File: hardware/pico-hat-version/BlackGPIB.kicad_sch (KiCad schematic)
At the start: 7 parts, among them J1 SD_Card_Module, J2 Raspberry_Pi_Connector

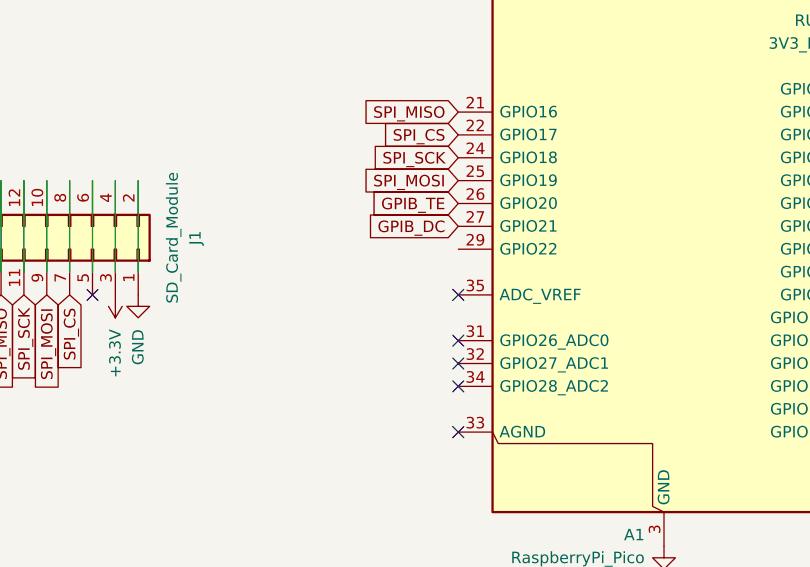
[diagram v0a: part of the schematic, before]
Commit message: fix pico hatted version: swap dc te and fix dc te on schematic
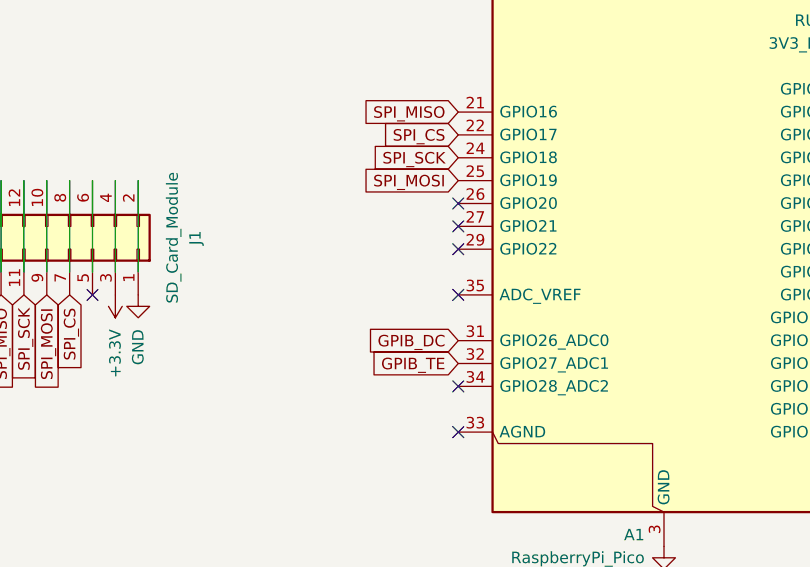
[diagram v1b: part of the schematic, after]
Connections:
- net GPIB_DC: now also A1.31 (GPIO26_ADC0); no longer A1.27 (GPIO21)
- net GPIB_TE: now also A1.32 (GPIO27_ADC1); no longer A1.26 (GPIO20)
- no-connect marks 8 -> 9

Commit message: pcb
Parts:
- A1: footprint Module:RaspberryPi_Pico_Common_Unspecified -> Module:RaspberryPi_Pico_W_SMD_HandSolder
- J1: footprint (none) -> Connector_PinHeader_2.54mm:PinHeader_2x08_P2.54mm_Vertical_SMD
- J2: footprint (none) -> Connector_PinHeader_2.54mm:PinHeader_2x20_P2.54mm_Vertical_SMD
- RN1, RN4: footprint Resistor_THT:R_Array_SIP9 -> custom:PinHeader_1x09_P2.54mm_Horizontal_Left
- RN2, RN3: footprint Resistor_THT:R_Array_SIP9 -> custom:PinHeader_1x09_P2.54mm_Horizontal_Right
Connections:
- net +3.3V: now also J1.4 (3.3V); no longer J2.1 (3.3V), J2.17 (3.3V)
- net GND: now also J1.16 (GND), J1.2 (GND)
- net SPI_CS: now also J1.8 (CS)
- net SPI_MISO: now also J1.14 (MISO)
- net SPI_MOSI: now also J1.10 (MOSI)
- net SPI_SCK: now also J1.12 (SCK)
- no-connect marks 9 -> 12
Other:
- moved on the sheet: J2

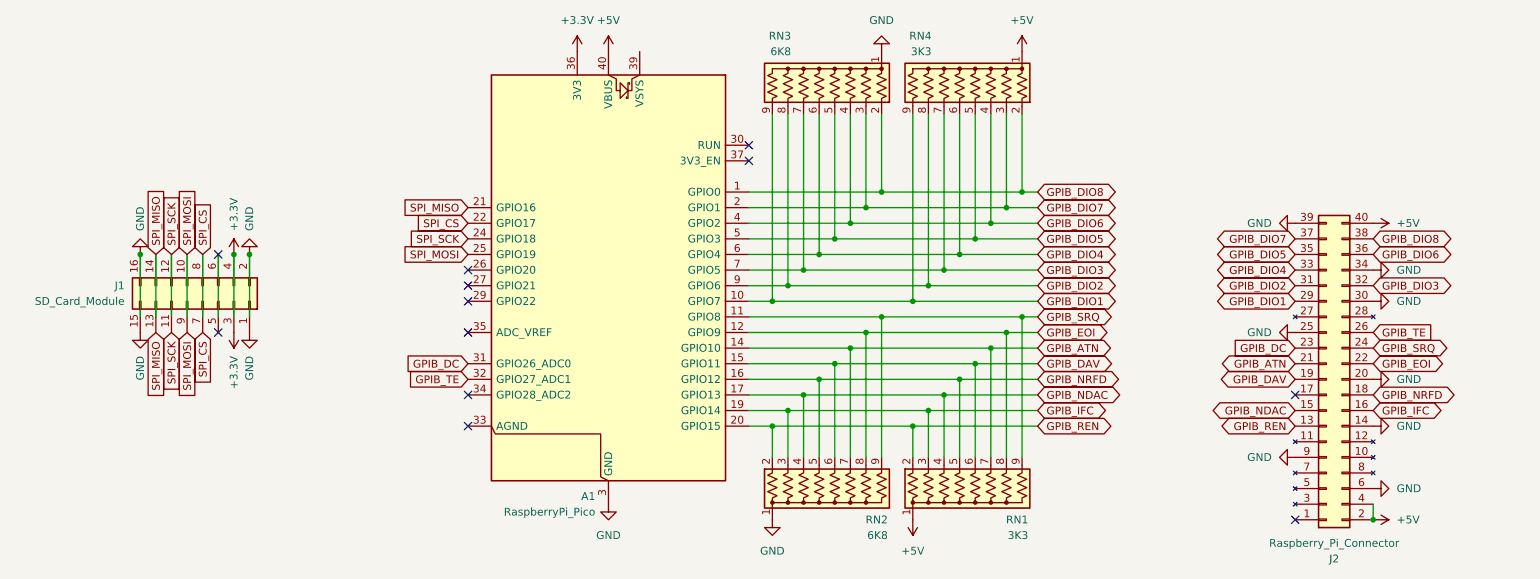
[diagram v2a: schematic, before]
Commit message: fix voltage divider for pico hat hardware
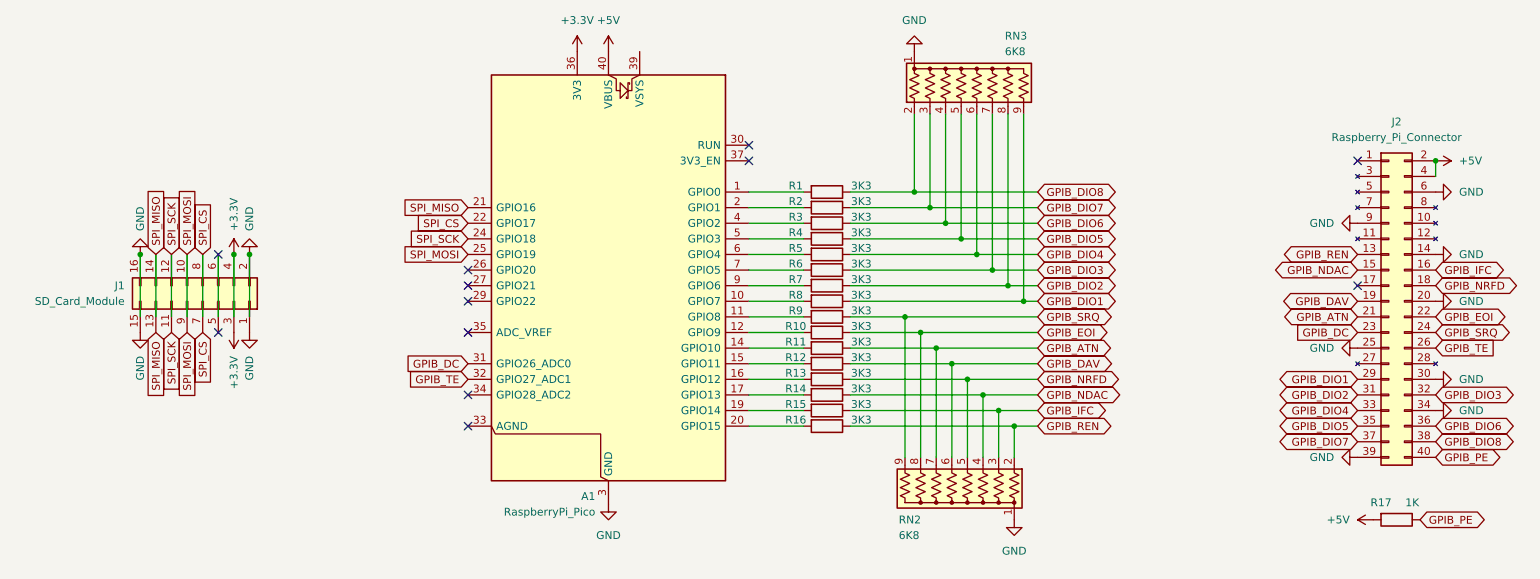
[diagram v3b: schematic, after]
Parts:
- removed RN1, RN4: 3K3, custom:PinHeader_1x09_P2.54mm_Horizontal_Left, symbol Device:R_Network08_US
- added R1, R10, R11, R12, R13, R14, R15, R16, R2, R3, R4, R5, R6, R7, R8, R9: 3K3, Resistor_SMD:R_0805_2012Metric_Pad1.20x1.40mm_HandSolder, symbol Device:R
- added R17: 1K, Resistor_SMD:R_0805_2012Metric_Pad1.20x1.40mm_HandSolder, symbol Device:R
- RN2: footprint custom:PinHeader_1x09_P2.54mm_Horizontal_Right -> custom:PinHeader_1x09_P2.54mm_Horizontal_Right_FlipX
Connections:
- net +5V: now also R17.2; no longer J2.40 (PE)
- net GPIB_ATN: now also R11.1; no longer A1.14 (GPIO10)
- net GPIB_DAV: now also R12.1; no longer A1.15 (GPIO11)
- net GPIB_DIO1: now also R8.1; no longer A1.10 (GPIO7)
- net GPIB_DIO2: now also R7.1; no longer A1.9 (GPIO6)
- net GPIB_DIO3: now also R6.1; no longer A1.7 (GPIO5)
- net GPIB_DIO4: now also R5.1; no longer A1.6 (GPIO4)
- net GPIB_DIO5: now also R4.1; no longer A1.5 (GPIO3)
- net GPIB_DIO6: now also R3.1; no longer A1.4 (GPIO2)
- net GPIB_DIO7: now also R2.1; no longer A1.2 (GPIO1)
- net GPIB_DIO8: now also R1.1; no longer A1.1 (GPIO0)
- net GPIB_EOI: now also R10.1; no longer A1.12 (GPIO9)
- net GPIB_IFC: now also R15.1; no longer A1.19 (GPIO14)
- net GPIB_NDAC: now also R14.1; no longer A1.17 (GPIO13)
- net GPIB_NRFD: now also R13.1; no longer A1.16 (GPIO12)
- net GPIB_REN: now also R16.1; no longer A1.20 (GPIO15)
- net GPIB_SRQ: now also R9.1; no longer A1.11 (GPIO8)
- new net: A1.7 (GPIO5), R6.2
- new net: A1.20 (GPIO15), R16.2
- new net: A1.19 (GPIO14), R15.2
- new net: A1.11 (GPIO8), R9.2
- new net: A1.10 (GPIO7), R8.2
- new net: A1.2 (GPIO1), R2.2
- new net: A1.15 (GPIO11), R12.2
- new net: A1.1 (GPIO0), R1.2
- new net: A1.4 (GPIO2), R3.2
- new net: A1.6 (GPIO4), R5.2
- new net: A1.5 (GPIO3), R4.2
- new net: A1.9 (GPIO6), R7.2
- new net: A1.12 (GPIO9), R10.2
- new net: A1.14 (GPIO10), R11.2
- new net: A1.16 (GPIO12), R13.2
- new net: A1.17 (GPIO13), R14.2
- new net GPIB_PE: J2.40 (PE), R17.1
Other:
- moved on the sheet: J2, RN2, RN3

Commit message: pico: optimize hatted version for SLA printer, remove optional components
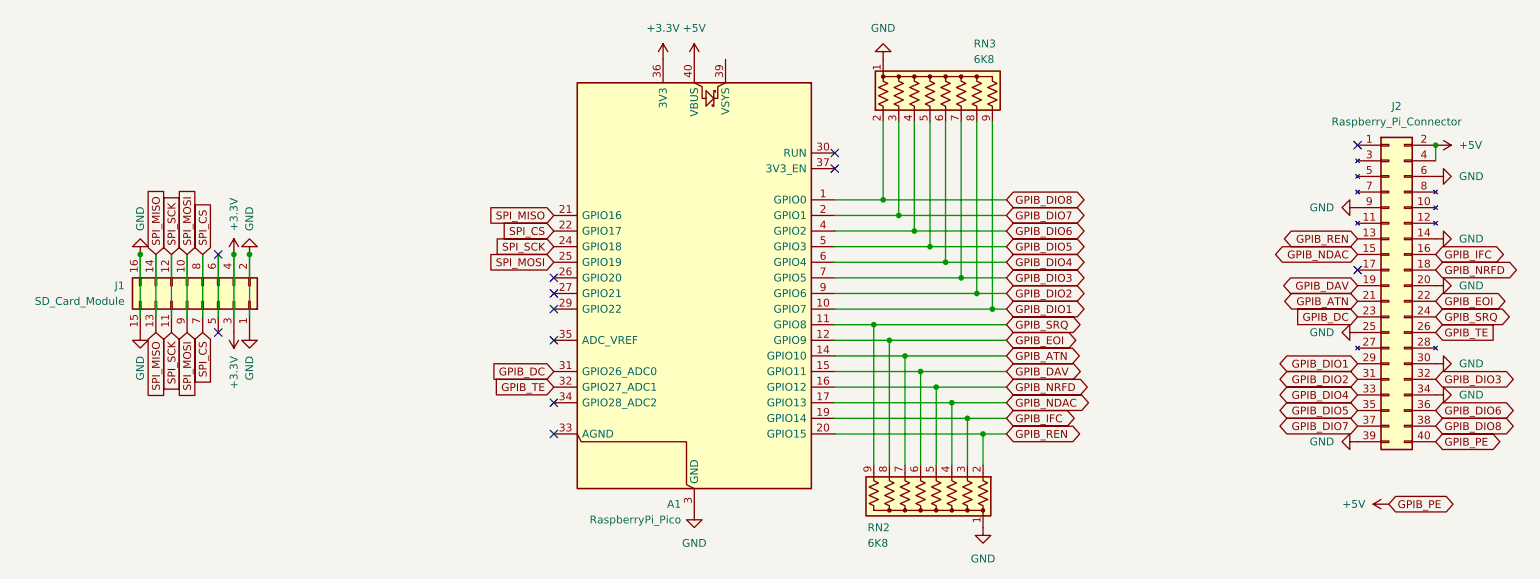
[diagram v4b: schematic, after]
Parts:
- removed R1, R10, R11, R12, R13, R14, R15, R16, R2, R3, R4, R5, R6, R7, R8, R9: 3K3, Resistor_SMD:R_0805_2012Metric_Pad1.20x1.40mm_HandSolder, symbol Device:R
- removed R17: 1K, Resistor_SMD:R_0805_2012Metric_Pad1.20x1.40mm_HandSolder, symbol Device:R
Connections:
- net GPIB_PE is gone; now on net +5V: J2.40 (PE)
- net GPIB_ATN: now also A1.14 (GPIO10)
- net GPIB_DAV: now also A1.15 (GPIO11)
- net GPIB_DIO1: now also A1.10 (GPIO7)
- net GPIB_DIO2: now also A1.9 (GPIO6)
- net GPIB_DIO3: now also A1.7 (GPIO5)
- net GPIB_DIO4: now also A1.6 (GPIO4)
- net GPIB_DIO5: now also A1.5 (GPIO3)
- net GPIB_DIO6: now also A1.4 (GPIO2)
- net GPIB_DIO7: now also A1.2 (GPIO1)
- net GPIB_DIO8: now also A1.1 (GPIO0)
- net GPIB_EOI: now also A1.12 (GPIO9)
- net GPIB_IFC: now also A1.19 (GPIO14)
- net GPIB_NDAC: now also A1.17 (GPIO13)
- net GPIB_NRFD: now also A1.16 (GPIO12)
- net GPIB_REN: now also A1.20 (GPIO15)
- net GPIB_SRQ: now also A1.11 (GPIO8)
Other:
- moved on the sheet: A1, J2, RN2, RN3
